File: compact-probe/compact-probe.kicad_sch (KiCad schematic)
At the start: 28 parts, among them J1 Conn_02x05_Counter_Clockwise, J2 SM04B-SRSS-TB(LF)(SN), J3 SM04B-SRSS-TB(LF)(SN), U1 TruStability_SPI, U2 TruStability_SPI, U3 TruStability_SPI, U4 ESP32-C3-WROOM-02-H4, U5 BMP388, U6 LT1963AxST-3.3, X1 baro_cap

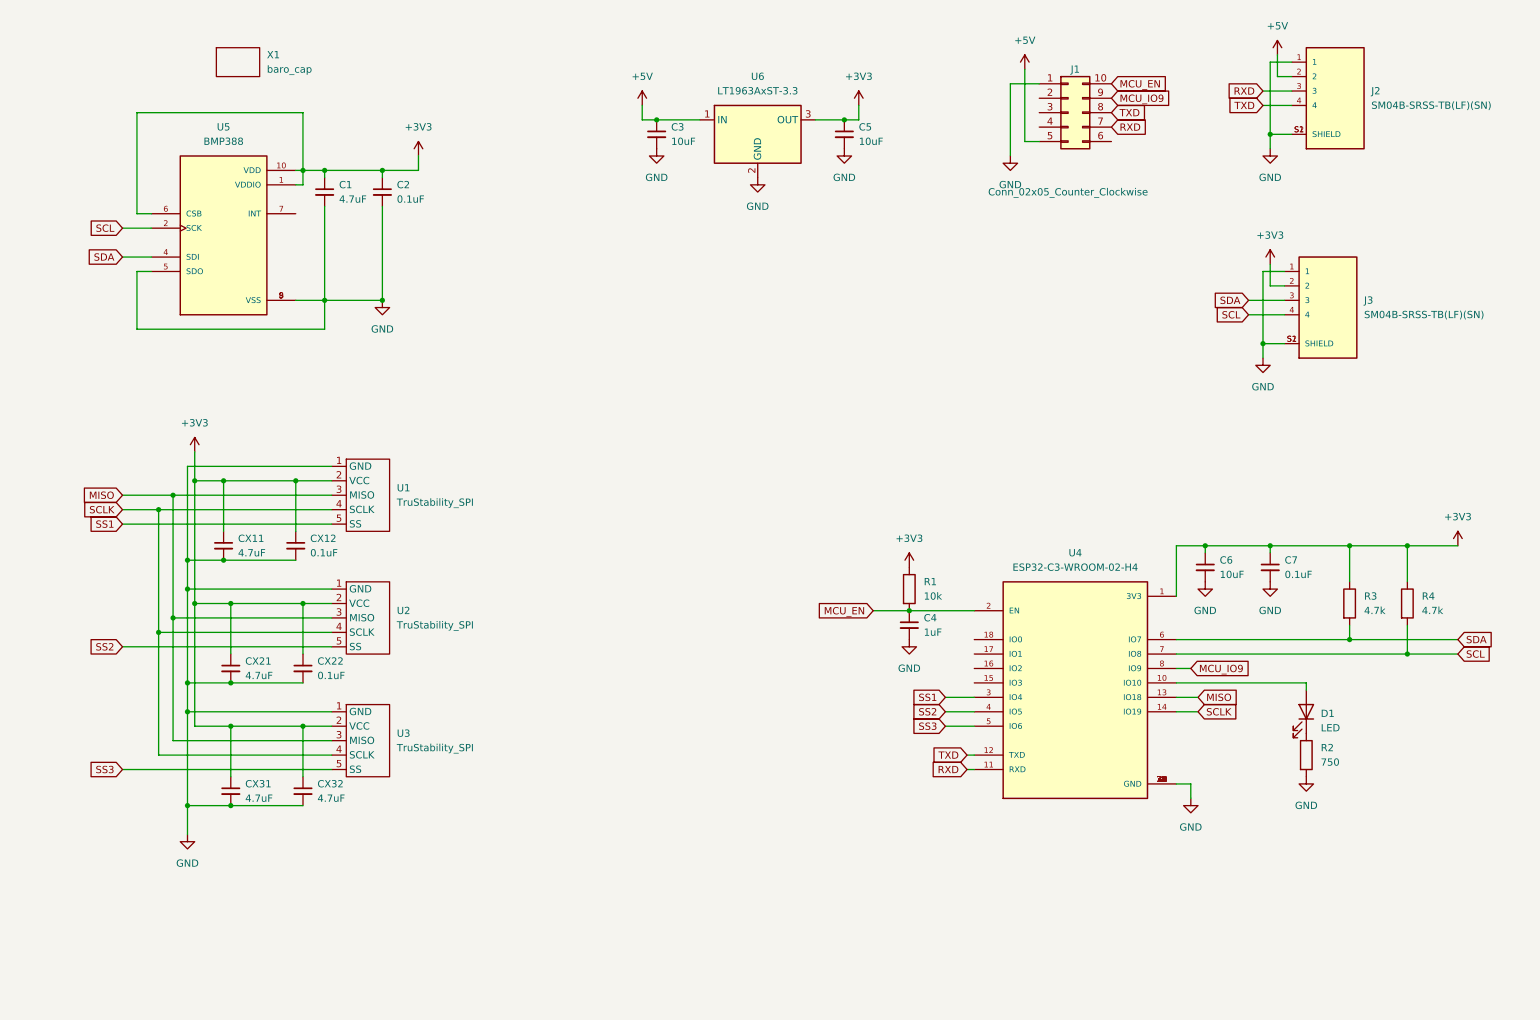
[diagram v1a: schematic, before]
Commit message: Finished first cut of routing.
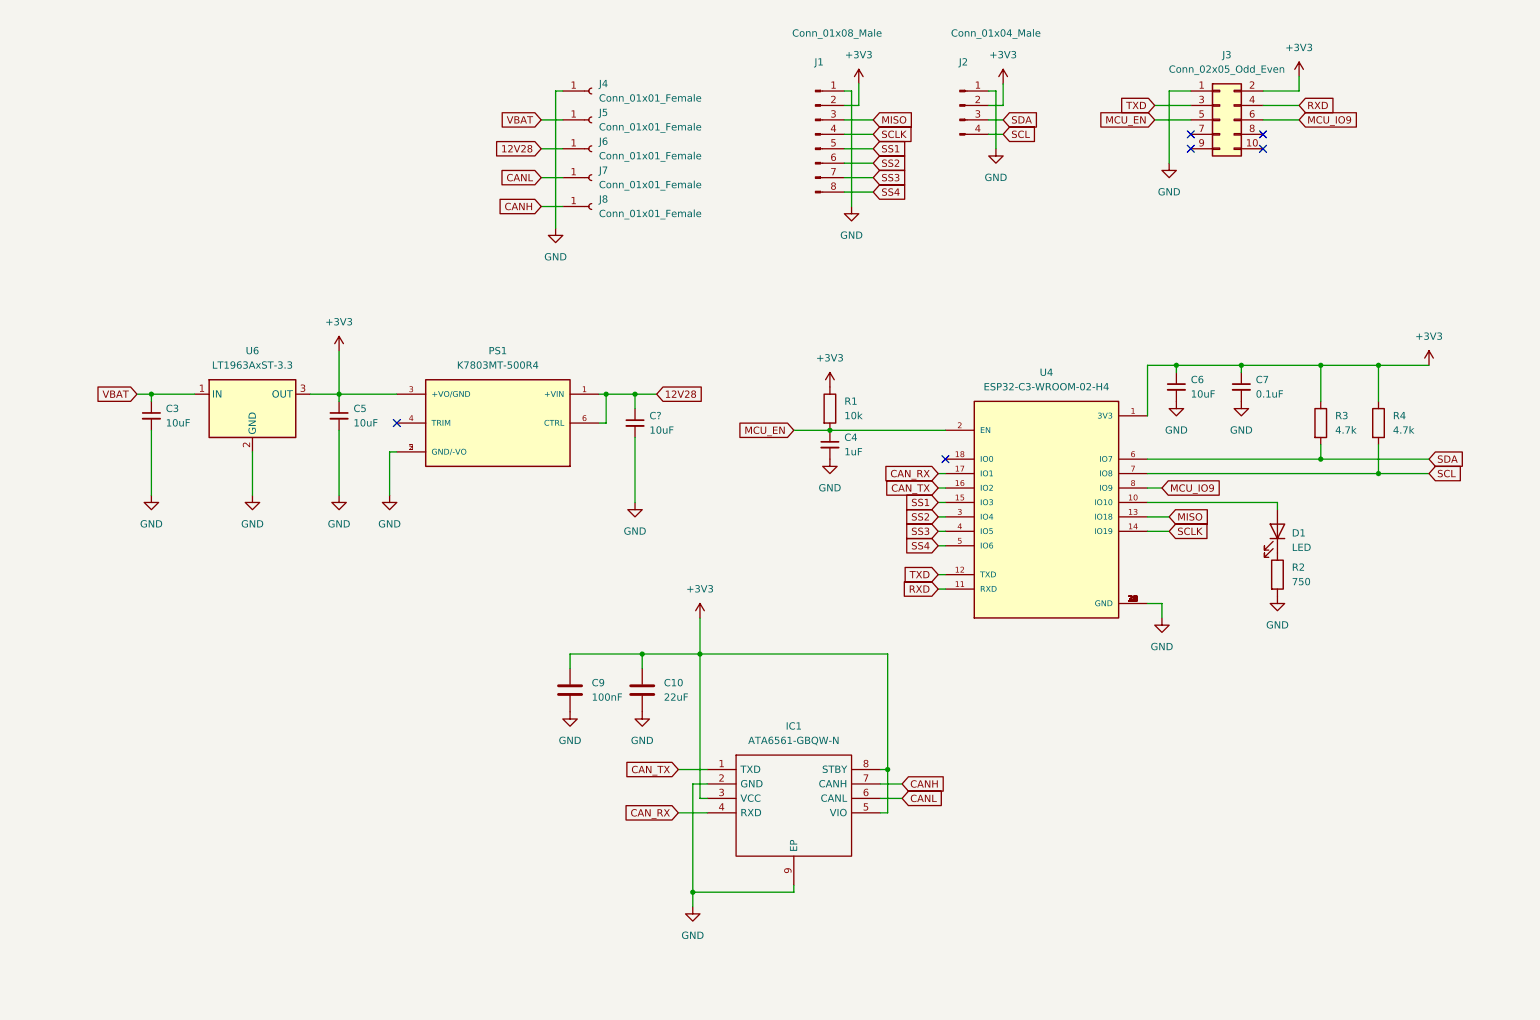
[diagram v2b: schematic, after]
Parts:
- removed C1, CX11, CX21, CX31, CX32: 4.7uF, Capacitor_SMD:C_0603_1608Metric, symbol Device:C_Small
- removed C2, CX12, CX22: 0.1uF, Capacitor_SMD:C_0603_1608Metric, symbol Device:C_Small
- removed J1: Conn_02x05_Counter_Clockwise, compact-probe:1.27mm_02x05_header, symbol Connector_Generic:Conn_02x05_Counter_Clockwise
- removed J2, J3: SM04B-SRSS-TB(LF)(SN), compact-probe:JST_SM04B-SRSS-TB(LF)(SN), symbol compact-probe:SM04B-SRSS-TB(LF)(SN)
- removed U1, U2, U3: TruStability_SPI, compact-probe:TruStability SMT, symbol compact-probe:TruStability_SPI
- removed U5: BMP388, compact-probe:BMP388, symbol compact-probe:BMP388
- removed X1: baro_cap, compact-probe:baro_cap, symbol compact-probe:baro_cap
- added C10: 22uF, Capacitor_SMD:C_0603_1608Metric, symbol Device:C
- added C9: 100nF, Capacitor_SMD:C_0603_1608Metric, symbol Device:C
- added C?: 10uF, Capacitor_SMD:C_0603_1608Metric, symbol Device:C_Small
- added IC1: ATA6561-GBQW-N, airball-hardware:SON65P300X300X90-9N-D, symbol airball-hardware:ATA6561-GBQW-N
- added J1: Conn_01x08_Male, airball-hardware:JST_SH_SM08B-SRSS-TB_1x08-1MP_P1.00mm_Horizontal, symbol Connector:Conn_01x08_Male
- added J2: Conn_01x04_Male, airball-hardware:JST_SM04B-SRSS-TB(LF)(SN), symbol Connector:Conn_01x04_Male
- added J3: Conn_02x05_Odd_Even, Connector_PinHeader_1.27mm:PinHeader_2x05_P1.27mm_Vertical, symbol Connector_Generic:Conn_02x05_Odd_Even
- added J4, J5, J6, J7, J8: Conn_01x01_Female, Connector_Wire:SolderWirePad_1x01_SMD_1x2mm, symbol Connector:Conn_01x01_Female
- added PS1: K7803MT-500R4, airball-hardware:CONV_K7803MT-500R4, symbol airball-hardware:K7803MT-500R4
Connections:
- net +3V3: now also C10.1, C9.1, IC1.3 (VCC), IC1.5 (VIO), IC1.8 (STBY), J1.2 (Pin_2), J2.2 (Pin_2), J3.2 (Pin_2), PS1.3 (+VO/GND)
- net GND: now also C10.2, C9.2, C?.2, IC1.2 (GND), IC1.9 (EP), J1.1 (Pin_1), J2.1 (Pin_1), J3.1 (Pin_1), J4.1 (Pin_1), PS1.2 (GND/-VO), PS1.5 (GND/-VO)
- net MCU_EN: now also J3.5 (Pin_5)
- net MCU_IO9: now also J3.6 (Pin_6)
- net MISO: now also J1.3 (Pin_3)
- net RXD: now also J3.4 (Pin_4)
- net SCL: now also J2.4 (Pin_4)
- net SCLK: now also J1.4 (Pin_4)
- net SDA: now also J2.3 (Pin_3)
- net SS1: now also U4.15 (IO3), J1.5 (Pin_5); no longer U4.3 (IO4)
- net SS2: now also U4.3 (IO4), J1.6 (Pin_6); no longer U4.4 (IO5)
- net SS3: now also U4.4 (IO5), J1.7 (Pin_7); no longer U4.5 (IO6)
- net TXD: now also J3.3 (Pin_3)
- net CAN_TX: now reaches U4.16 (IO2)
- net CAN_TX: now also IC1.1 (TXD)
- net CAN_RX: now reaches U4.17 (IO1)
- net CAN_RX: now also IC1.4 (RXD)
- net +5V renamed VBAT
- net VBAT: now also J5.1 (Pin_1)
- new net 12V28: C?.1, J6.1 (Pin_1), PS1.1 (+VIN), PS1.6 (CTRL)
- new net CANH: IC1.7 (CANH), J8.1 (Pin_1)
- new net CANL: IC1.6 (CANL), J7.1 (Pin_1)
- new net SS4: J1.8 (Pin_8), U4.5 (IO6)
- no-connect marks 0 -> 6
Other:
- moved on the sheet: C3, C4, C5, C6, C7, D1, R1, R2, R3, R4, U4, U6

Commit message: Final changes.
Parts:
- gave numbers to parts that had none: 1
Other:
- moved on the sheet: C1, C10, C3, C5, C9, IC1, PS1, U6

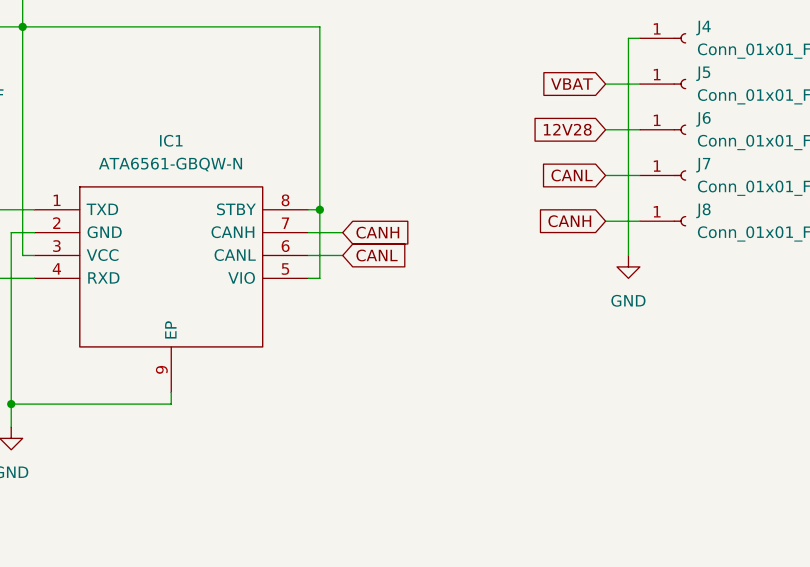
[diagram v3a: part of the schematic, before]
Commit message: Added CANBus 120 ohm termination resistor.
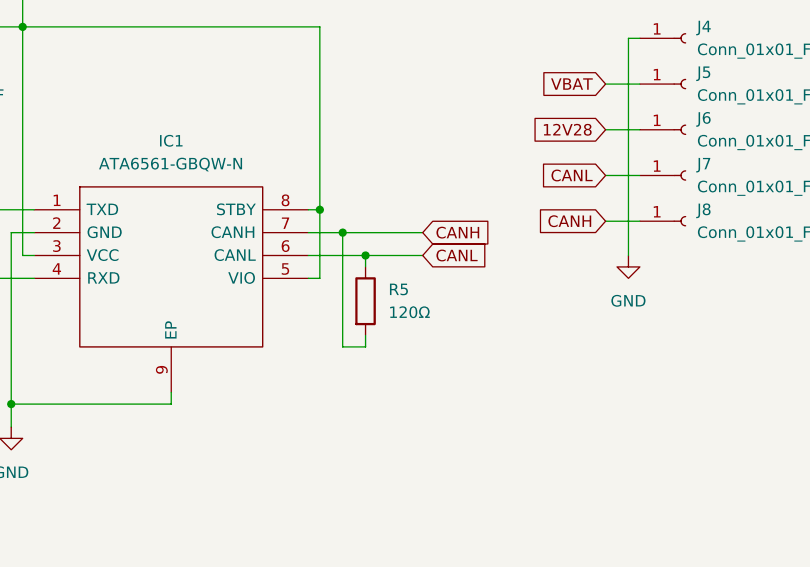
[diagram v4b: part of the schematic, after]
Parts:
- added R5: 120Ω, Resistor_SMD:R_0603_1608Metric, symbol Device:R
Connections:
- net CANH: now also R5.2
- net CANL: now also R5.1
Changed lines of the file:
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@@
   (junction (at 246.38 76.2) (diameter 0) (color 0 0 0 0)
   )
+  (junction (at 82.55 52.07) (diameter 0) (color 0 0 0 0)
+  )
   (junction (at 160.02 87.63) (diameter 0) (color 0 0 0 0)
   )
@@
   )
   (junction (at 220.98 76.2) (diameter 0) (color 0 0 0 0)
+  )
+  (junction (at 80.01 49.53) (diameter 0) (color 0 0 0 0)
   )
   (no_connect (at 180.34 92.71))
@@
     (stroke (width 0) (type default) (color 0 0 0 0))
   )
-  (wire (pts (xy 76.2 52.07) (xy 80.01 52.07))
+  (wire (pts (xy 76.2 52.07) (xy 82.55 52.07))
     (stroke (width 0) (type default) (color 0 0 0 0))
   )
@@
     (stroke (width 0) (type default) (color 0 0 0 0))
   )
+  (wire (pts (xy 82.55 60.96) (xy 82.55 62.23))
+    (stroke (width 0) (type default) (color 0 0 0 0))
+  )
   (wire (pts (xy 190.5 26.67) (xy 190.5 30.48))
     (stroke (width 0) (type default) (color 0 0 0 0))
@@
     (stroke (width 0) (type default) (color 0 0 0 0))
   )
+  (wire (pts (xy 82.55 52.07) (xy 82.55 53.34))
+    (stroke (width 0) (type default) (color 0 0 0 0))
+  )
   (wire (pts (xy 246.38 90.17) (xy 246.38 92.71))
     (stroke (width 0) (type default) (color 0 0 0 0))
@@
     (stroke (width 0) (type default) (color 0 0 0 0))
   )
+  (wire (pts (xy 80.01 49.53) (xy 80.01 62.23))
+    (stroke (width 0) (type default) (color 0 0 0 0))
+  )
   (wire (pts (xy 115.57 172.72) (xy 115.57 182.88))
     (stroke (width 0) (type default) (color 0 0 0 0))
@@
     (stroke (width 0) (type default) (color 0 0 0 0))
   )
+  (wire (pts (xy 82.55 52.07) (xy 88.9 52.07))
+    (stroke (width 0) (type default) (color 0 0 0 0))
+  )
   (wire (pts (xy 189.23 27.94) (xy 189.23 38.1))
     (stroke (width 0) (type default) (color 0 0 0 0))
@@
     (stroke (width 0) (type default) (color 0 0 0 0))
   )
+  (wire (pts (xy 80.01 49.53) (xy 88.9 49.53))
+    (stroke (width 0) (type default) (color 0 0 0 0))
+  )
   (wire (pts (xy 34.29 26.67) (xy 21.59 26.67))
     (stroke (width 0) (type default) (color 0 0 0 0))
@@
     (stroke (width 0) (type default) (color 0 0 0 0))
   )
+  (wire (pts (xy 82.55 62.23) (xy 80.01 62.23))
+    (stroke (width 0) (type default) (color 0 0 0 0))
+  )
   (wire (pts (xy 256.54 95.25) (xy 265.43 95.25))
     (stroke (width 0) (type default) (color 0 0 0 0))
@@
     )
   )
-  (global_label "CANL" (shape input) (at 80.01 52.07 0) (fields_autoplaced)
-    (effects (font (size 1.27 1.27)) (justify left))
-    (property "Intersheet References" "${INTERSHEET_REFS}" (id 0) (at 87.1402 51.9906 0)
+  (global_label "CANL" (shape input) (at 88.9 52.07 0) (fields_autoplaced)
+    (effects (font (size 1.27 1.27)) (justify left))
+    (property "Intersheet References" "${INTERSHEET_REFS}" (id 0) (at 96.0302 51.9906 0)
       (effects (font (size 1.27 1.27)) (justify left) hide)
     )
@@
     )
   )
-  (global_label "CANH" (shape input) (at 80.01 49.53 0) (fields_autoplaced)
-    (effects (font (size 1.27 1.27)) (justify left))
-    (property "Intersheet References" "${INTERSHEET_REFS}" (id 0) (at 87.4426 49.4506 0)
+  (global_label "CANH" (shape input) (at 88.9 49.53 0) (fields_autoplaced)
+    (effects (font (size 1.27 1.27)) (justify left))
+    (property "Intersheet References" "${INTERSHEET_REFS}" (id 0) (at 96.3326 49.4506 0)
       (effects (font (size 1.27 1.27)) (justify left) hide)
     )
@@
     (pin "1")
   )
+  (symbol (lib_id "Device:R") (at 82.55 57.15 0) (unit 1)
+    (in_bom yes) (on_board yes) (fields_autoplaced)
+    (property "Reference" "R5" (id 0) (at 85.09 55.8799 0)
+      (effects (font (size 1.27 1.27)) (justify left))
+    )
+    (property "Value" "120Ω" (id 1) (at 85.09 58.4199 0)
+      (effects (font (size 1.27 1.27)) (justify left))
+    )
+    (property "Footprint" "Resistor_SMD:R_0603_1608Metric" (id 2) (at 80.772 57.15 90)
+      (effects (font (size 1.27 1.27)) hide)
+    )
+    (property "Datasheet" "~" (id 3) (at 82.55 57.15 0)
+      (effects (font (size 1.27 1.27)) hide)
+    )
+    (pin "1")
+    (pin "2")
+  )
   (symbol (lib_name "GND_3") (lib_id "power:GND") (at 72.39 182.88 0) (mirror y) (unit 1)
     (in_bom yes) (on_board yes) (fields_autoplaced)
@@
       (reference "R4") (unit 1) (value "4.7k") (footprint "Resistor_SMD:R_0603_1608Metric")
     )
+    (path "/d9b62351-898a-4655-849a-9f4f68314e7f"
+      (reference "R5") (unit 1) (value "120Ω") (footprint "Resistor_SMD:R_0603_1608Metric")
+    )
     (path "/8ee1f2b1-be92-4b22-ae06-e4e6ff025983"

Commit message: Finished design & created fab outputs.
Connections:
- net VBAT: now also J3.7 (Pin_7)
- no-connect marks 6 -> 5
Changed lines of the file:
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@@
   (no_connect (at 180.34 92.71))
   (no_connect (at 73.66 170.18))
-  (no_connect (at 223.52 35.56))
   (no_connect (at 236.22 35.56))
   (no_connect (at 223.52 38.1))
@@
     (stroke (width 0) (type default) (color 0 0 0 0))
   )
+  (wire (pts (xy 241.3 24.13) (xy 241.3 27.94))
+    (stroke (width 0) (type default) (color 0 0 0 0))
+  )
   (wire (pts (xy 215.9 95.25) (xy 256.54 95.25))
     (stroke (width 0) (type default) (color 0 0 0 0))
@@
     (stroke (width 0) (type default) (color 0 0 0 0))
   )
-  (wire (pts (xy 236.22 27.94) (xy 242.57 27.94))
-    (stroke (width 0) (type default) (color 0 0 0 0))
-  )
   (wire (pts (xy 60.96 67.31) (xy 60.96 68.58))
     (stroke (width 0) (type default) (color 0 0 0 0))
@@
     (stroke (width 0) (type default) (color 0 0 0 0))
   )
+  (wire (pts (xy 217.17 35.56) (xy 223.52 35.56))
+    (stroke (width 0) (type default) (color 0 0 0 0))
+  )
   (wire (pts (xy 111.76 27.94) (xy 111.76 52.07))
     (stroke (width 0) (type default) (color 0 0 0 0))
@@
     (stroke (width 0) (type default) (color 0 0 0 0))
   )
-  (wire (pts (xy 242.57 25.4) (xy 242.57 27.94))
-    (stroke (width 0) (type default) (color 0 0 0 0))
-  )
   (wire (pts (xy 238.76 100.33) (xy 238.76 101.6))
     (stroke (width 0) (type default) (color 0 0 0 0))
@@
     (stroke (width 0) (type default) (color 0 0 0 0))
   )
+  (wire (pts (xy 241.3 27.94) (xy 236.22 27.94))
+    (stroke (width 0) (type default) (color 0 0 0 0))
+  )
   (wire (pts (xy 63.5 171.45) (xy 63.5 182.88))
     (stroke (width 0) (type default) (color 0 0 0 0))
@@
     (property "Intersheet References" "${INTERSHEET_REFS}" (id 0) (at 248.7326 30.4006 0)
       (effects (font (size 1.27 1.27)) (justify left) hide)
+    )
+  )
+  (global_label "VBAT" (shape input) (at 217.17 35.56 180) (fields_autoplaced)
+    (effects (font (size 1.27 1.27)) (justify right))
+    (property "Intersheet References" "${INTERSHEET_REFS}" (id 0) (at 210.3421 35.4806 0)
+      (effects (font (size 1.27 1.27)) (justify right) hide)
     )
   )
@@
     (pin "1")
   )
-  (symbol (lib_name "+3V3_2") (lib_id "power:+3V3") (at 242.57 25.4 0) (unit 1)
-    (in_bom yes) (on_board yes) (fields_autoplaced)
-    (property "Reference" "#PWR0111" (id 0) (at 242.57 29.21 0)
-      (effects (font (size 1.27 1.27)) hide)
-    )
-    (property "Value" "+3V3" (id 1) (at 242.57 20.32 0))
-    (property "Footprint" "" (id 2) (at 242.57 25.4 0)
-      (effects (font (size 1.27 1.27)) hide)
-    )
-    (property "Datasheet" "" (id 3) (at 242.57 25.4 0)
-      (effects (font (size 1.27 1.27)) hide)
-    )
-    (pin "1")
-  )
   (symbol (lib_name "GND_3") (lib_id "power:GND") (at 115.57 182.88 0) (mirror y) (unit 1)
     (in_bom yes) (on_board yes) (fields_autoplaced)
@@
     (pin "2")
   )
+  (symbol (lib_id "power:+3V3") (at 241.3 24.13 0) (unit 1)
+    (in_bom yes) (on_board yes) (fields_autoplaced)
+    (property "Reference" "#PWR?" (id 0) (at 241.3 27.94 0)
+      (effects (font (size 1.27 1.27)) hide)
+    )
+    (property "Value" "+3V3" (id 1) (at 241.3 19.05 0))
+    (property "Footprint" "" (id 2) (at 241.3 24.13 0)
+      (effects (font (size 1.27 1.27)) hide)
+    )
+    (property "Datasheet" "" (id 3) (at 241.3 24.13 0)
+      (effects (font (size 1.27 1.27)) hide)
+    )
+    (pin "1")
+  )
   (symbol (lib_id "Device:C") (at 21.59 33.02 0) (unit 1)
     (in_bom yes) (on_board yes)
@@
       (reference "#PWR0110") (unit 1) (value "GND") (footprint "")
     )
-    (path "/a2476a88-d6a2-43dd-942d-f24a3baa81f1"
-      (reference "#PWR0111") (unit 1) (value "+3V3") (footprint "")
-    )
     (path "/17596dc0-4315-415e-aa9a-e6b81ac8ff05"
       (reference "#PWR0112") (unit 1) (value "GND") (footprint "")
@@
       (reference "#PWR0115") (unit 1) (value "GND") (footprint "")
     )
+    (path "/e9d79e68-1fa1-4ac6-9ab2-434e3106c0b2"
+      (reference "#PWR?") (unit 1) (value "+3V3") (footprint "")
+    )
     (path "/67b7b974-aeb8-4105-b89a-321d2a2551f9"
